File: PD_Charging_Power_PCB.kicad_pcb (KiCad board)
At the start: 2 copper layers, 28 x 30 mm, 34 parts, among them J1 105450-0101, Q1 CJQ4459, Q2 2N7002KDW, U1 STUSB4500

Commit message: Ruan: modify for V0.1
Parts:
- moved INT1 8.96 mm to (121.8, 146.8)
- moved TP8 7.72 mm to (127.8, 139.4), turned to 0 degrees
- moved SDA1 2.69 mm to (122.7, 141.3)
- moved D4 2.31 mm to (131.6, 142.5), turned to 0 degrees
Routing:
- net GND: track 107.8 -> 81.1 mm
- net Net-(C6-Pad1): track 31.1 -> 45.0 mm
- net Net-(INT1-Pad1): track 18.6 -> 23.2 mm
- net Net-(SDA1-Pad1): track 9.63 -> 6.75 mm

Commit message: Ruan: base ok V0.1
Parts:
- removed TP1: GND, TestPoint:TestPoint_Pad_D1.5mm
- added GND1: GND, TestPoint:TestPoint_Pad_D1.0mm, F.Cu at (51.7, 139.1)
- ABS1, Att1: moved to F.Cu
- C1, C2, C3, C4, C5, C6, D1, D2, D3, D4, Q1, R1, R10, R11, R2, R3, R4, R5, R6, R7, R8, R9, TP8, U1: moved to B.Cu
- CLK1, INT1, RST1, SDA1, VBUS1: footprint TestPoint:TestPoint_Pad_D1.5mm -> TestPoint:TestPoint_Pad_D1.0mm; moved to F.Cu
- J1: footprint RuanProject:MOLEX_105450-0101_modifyed -> RuanProject:MOLEX_105450-0101
- Q2: footprint digikey-footprints:SOT-363 -> RuanProject:SOT-363_SC-70-6; moved to B.Cu
- moved VBUS1 75.9 mm to (51.7, 141.7)
- moved Q1 75.8 mm to (53.8, 159.6), turned to 270 degrees
- moved R6 75.8 mm to (57.5, 157.3), turned to 90 degrees
- moved D4 73.0 mm to (60.3, 158.2), turned to 90 degrees
- moved J1 72.7 mm to (42.2, 142.3), turned to 0 degrees
- moved RST1 69.0 mm to (56.1, 138.8)
- moved TP8 68.6 mm to (63.0, 162.1), turned to 90 degrees
- moved R7 68.3 mm to (55.8, 153.9), turned to 90 degrees
- moved CLK1 66.9 mm to (58.3, 139.8)
- moved R10 66.9 mm to (57.4, 153.9), turned to 270 degrees
- moved SDA1 66.2 mm to (56.5, 140.8)
- moved C6 64.7 mm to (59.8, 153.3)
- moved R3 64.5 mm to (56.0, 139.1), turned to 180 degrees
- moved D2 63.4 mm to (49.1, 139.8), turned to 90 degrees
- moved C1 62.4 mm to (49.0, 142.8), turned to 90 degrees
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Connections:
- J1 pad S1: Net-(J1-PadS1) -> GND
- J1 pad S2: Net-(J1-PadS1) -> GND
- J1 pad S3: Net-(J1-PadS1) -> GND
- J1 pad S4: Net-(J1-PadS1) -> GND
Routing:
- net GND: track 81.1 -> 105.7 mm, vias 38 -> 34
- net Net-(INT1-Pad1): track 23.2 -> 3.66 mm
- net Net-(C6-Pad1): track 45.0 -> 28.3 mm
- net Net-(R11-Pad2): track 9.08 -> 21.5 mm
- net Net-(R5-Pad2): track 15.0 -> 2.92 mm
- net Net-(Q2-Pad6): track 8.52 -> 16.5 mm, vias 0 -> 2
- net Net-(CLK1-Pad1): track 9.51 -> 2.27 mm
- net Net-(R3-Pad1): track 11.3 -> 4.33 mm
- net Net-(Q1-Pad4): track 10.9 -> 6.09 mm
- net /CC2: track 19.7 -> 24.0 mm, vias 2 -> 1
- net Net-(ABS1-Pad1): track 6.19 -> 3.05 mm
- net Net-(R4-Pad2): track 7.92 -> 5.07 mm
- net /CC1: track 20.3 -> 22.7 mm, vias 2 -> 1
- net Net-(Att1-Pad1): track 4.37 -> 2.83 mm
- net VBUS: track 72.7 -> 73.8 mm, vias 1 -> 16
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- added copper zone on B.Cu, net Net-(C6-Pad1)
- added copper zone on B.Cu, net VBUS
- removed copper zone on F.Cu, net Net-(C6-Pad1)
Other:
- board size 28 x 30 mm -> 30 x 28 mm

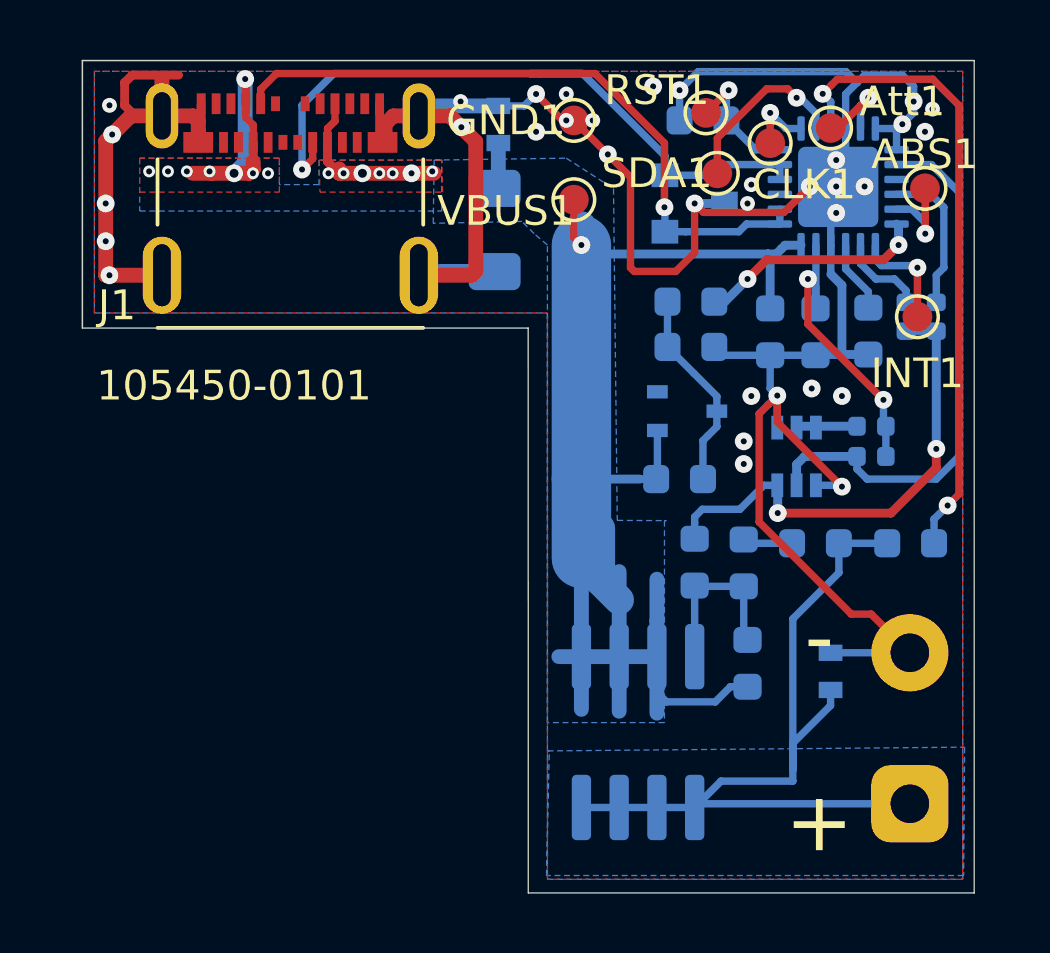
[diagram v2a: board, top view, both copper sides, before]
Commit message: Ruan: add treat drop
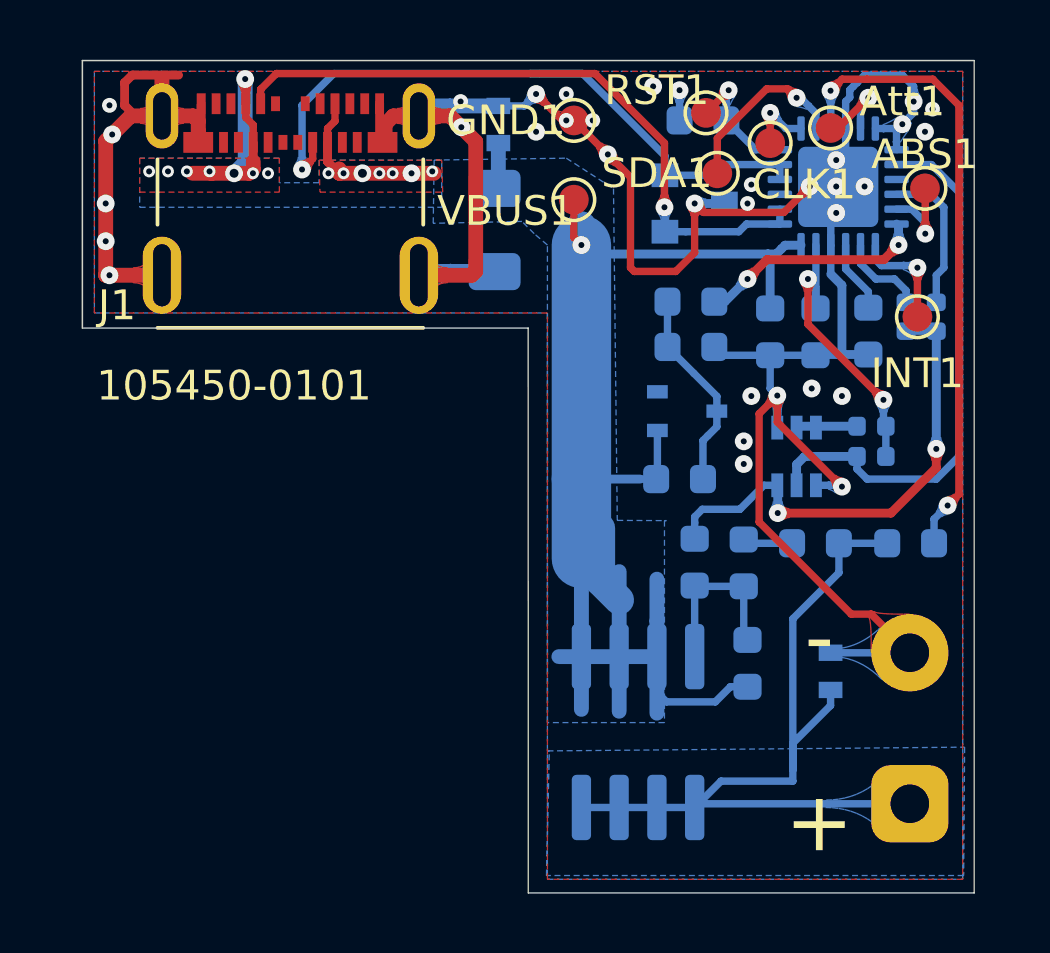
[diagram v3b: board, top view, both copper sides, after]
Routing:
- net GND: track 105.7 -> 99.4 mm

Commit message: Ruan；V0.1B
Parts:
- moved D2 4.71 mm to (49.5, 144.5), turned to 180 degrees
- moved VBUS1 4.38 mm to (53.5, 145.7)
- moved GND1 3.24 mm to (48.5, 139.2)
- moved C1 2.76 mm to (50.7, 140.6), turned to 270 degrees
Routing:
- net GND: track 99.4 -> 73.4 mm
- net /CC2: track 24.0 -> 18.2 mm
- net VBUS: track 73.8 -> 76.8 mm, vias 16 -> 18
- net /CC1: track 22.7 -> 21.5 mm
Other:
- net class Default: via_dia 0.6 -> 0.5

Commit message: Ruan: update to V0.2
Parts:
- removed TP8: Power Soldering Pad, TestPoint:TestPoint_2Pads_Pitch5.08mm_Drill1.3mm
- added VOUT+1: VOUT+, RuanProject:TestPoint_Pad_4mmx3mm, B.Cu at (61.6, 156.8)
- added Vout-1: Vout-, RuanProject:TestPoint_Pad_4mmx3mm, B.Cu at (61.6, 162.7)
- moved D4 5.17 mm to (57.1, 162.3), turned to 270 degrees
- moved Q1 0.69 mm to (53.8, 159.0)
- moved R10 0.45 mm to (57.4, 153.5)
- moved R7 0.41 mm to (55.8, 153.5)
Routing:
- net VBUS: track 76.8 -> 51.2 mm
- net Net-(C6-Pad1): track 28.3 -> 6.71 mm
- net GND: track 73.4 -> 64.4 mm, vias 34 -> 54
- net Net-(Q2-Pad6): track 16.5 -> 19.6 mm, vias 2 -> 3
